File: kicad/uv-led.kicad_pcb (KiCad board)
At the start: 2 copper layers, 100 x 8 mm, 9 parts, among them J1 JST_PH_B2B-PH-K_1x02_P2.00mm_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

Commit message: added screw specs to silkscreen (#3)
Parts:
- H1, H2: footprint MountingHole:MountingHole_3.2mm_M3_DIN965_Pad_TopOnly -> MountingHole:MountingHole_3.2mm_M3_ISO14580_Pad_TopOnly
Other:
- board text added: "M3x10 ISO 14580 0.3 Nm"
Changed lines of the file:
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@@
 		(capping no)
 		(filling no)
-		(zone_defaults)
 		(pcbplotparams
 			(layerselection 0x00000000_00000000_55555555_5755f5ff)
@@
 		)
 	)
-	(footprint "MountingHole:MountingHole_3.2mm_M3_DIN965_Pad_TopOnly"
+	(footprint "MountingHole:MountingHole_3.2mm_M3_ISO14580_Pad_TopOnly"
 		(layer "F.Cu")
 		(at 190 100)
 		(descr "Mounting Hole 3.2mm, M3, generated by kicad-footprint-generator mountinghole.py")
-		(tags "mountinghole M3 DIN965")
+		(tags "mountinghole M3 ISO14580")
 		(property "Reference" "H2"
-			(at 5 0 0)
+			(at 0 -7 0)
 			(layer "F.SilkS")
 			(effects
@@
 		(property ki_fp_filters "MountingHole*Pad*")
 		(sheetname "/")
-		(sheetfile "uv-led-pcb.kicad_sch")
+		(sheetfile "uv-led.kicad_sch")
 		(units
 			(unit
@@
 		(fp_circle
 			(center 0 0)
-			(end 2.8 0)
+			(end 2.75 0)
 			(stroke
 				(width 0.15)
@@
 		(fp_circle
 			(center 0 0)
-			(end 3.05 0)
+			(end 3 0)
 			(stroke
 				(width 0.05)
@@
 		(pad "1" connect circle
 			(at 0 0)
-			(size 5.6 5.6)
+			(size 5.5 5.5)
 			(layers "F.Cu" "F.Mask")
 			(net "GND")
@@
 		(property ki_fp_filters "LED* LED_SMD:* LED_THT:*")
 		(sheetname "/")
-		(sheetfile "uv-led-pcb.kicad_sch")
+		(sheetfile "uv-led.kicad_sch")
 		(units
 			(unit
@@
 		(property ki_fp_filters "LED* LED_SMD:* LED_THT:*")
 		(sheetname "/")
-		(sheetfile "uv-led-pcb.kicad_sch")
+		(sheetfile "uv-led.kicad_sch")
 		(units
 			(unit
@@
 		(property ki_fp_filters "LED* LED_SMD:* LED_THT:*")
 		(sheetname "/")
-		(sheetfile "uv-led-pcb.kicad_sch")
+		(sheetfile "uv-led.kicad_sch")
 		(units
 			(unit
@@
 		(property ki_fp_filters "LED* LED_SMD:* LED_THT:*")
 		(sheetname "/")
-		(sheetfile "uv-led-pcb.kicad_sch")
+		(sheetfile "uv-led.kicad_sch")
 		(units
 			(unit
@@
 		(property ki_fp_filters "LED* LED_SMD:* LED_THT:*")
 		(sheetname "/")
-		(sheetfile "uv-led-pcb.kicad_sch")
+		(sheetfile "uv-led.kicad_sch")
 		(units
 			(unit
@@
 		)
 	)
-	(footprint "MountingHole:MountingHole_3.2mm_M3_DIN965_Pad_TopOnly"
+	(footprint "MountingHole:MountingHole_3.2mm_M3_ISO14580_Pad_TopOnly"
 		(layer "F.Cu")
 		(at 110 100)
 		(descr "Mounting Hole 3.2mm, M3, generated by kicad-footprint-generator mountinghole.py")
-		(tags "mountinghole M3 DIN965")
+		(tags "mountinghole M3 ISO14580")
 		(property "Reference" "H1"
-			(at -5 0 0)
+			(at 0 -5 0)
 			(layer "F.SilkS")
 			(effects
@@
 		(property ki_fp_filters "MountingHole*Pad*")
 		(sheetname "/")
-		(sheetfile "uv-led-pcb.kicad_sch")
+		(sheetfile "uv-led.kicad_sch")
 		(units
 			(unit
@@
 		(fp_circle
 			(center 0 0)
-			(end 2.8 0)
+			(end 2.75 0)
 			(stroke
 				(width 0.15)
@@
 		(fp_circle
 			(center 0 0)
-			(end 3.05 0)
+			(end 3 0)
 			(stroke
 				(width 0.05)
@@
 		(pad "1" connect circle
 			(at 0 0)
-			(size 5.6 5.6)
+			(size 5.5 5.5)
 			(layers "F.Cu" "F.Mask")
 			(net "GND")
@@
 		(property ki_fp_filters "R_*")
 		(sheetname "/")
-		(sheetfile "uv-led-pcb.kicad_sch")
+		(sheetfile "uv-led.kicad_sch")
 		(units
 			(unit
@@
 		(property ki_fp_filters "Connector*:*_1x??_*")
 		(sheetname "/")
-		(sheetfile "uv-led-pcb.kicad_sch")
+		(sheetfile "uv-led.kicad_sch")
 		(units
 			(unit
@@
 		(layer "Edge.Cuts")
 	)
+	(gr_text "M3x10\nISO 14580\n0.3 Nm"
+		(at 101.5 101.1 0)
+		(layer "F.SilkS")
+		(effects
+			(font
+				(size 0.5 0.5)
+				(thickness 0.1)
+			)
+			(justify left bottom)
+		)
+	)
+	(gr_text "M3x10\nISO 14580\n0.3 Nm"
+		(at 193.8 101.1 0)
+		(layer "F.SilkS")
+		(effects
+			(font
+				(size 0.5 0.5)
+				(thickness 0.1)
+			)
+			(justify left bottom)
+		)
+	)
 	(segment

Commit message: added recommended voltage / current and max current (#4)
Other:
- board text added: "20V / 0.5A max current: 1A"
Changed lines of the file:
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@@
+		)
+	)
+	(gr_text "20V / 0.5A\nmax current: 1A"
+		(at 117.4 101.2 0)
+		(layer "F.SilkS")
+		(effects
+			(font
+				(size 1 1)
+				(thickness 0.1)
+			)
+			(justify left bottom)
 		)
 	)

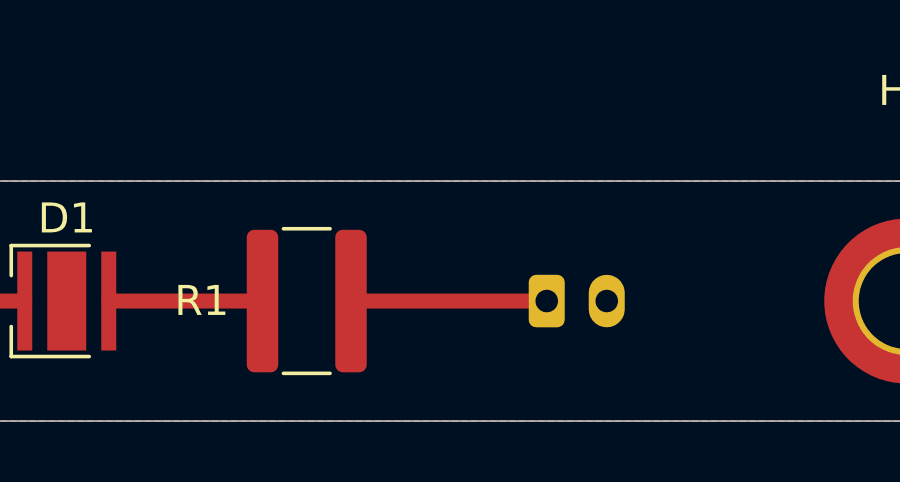
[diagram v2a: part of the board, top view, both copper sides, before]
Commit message: added polarity marker (+) on front and back silkscreen (#5)
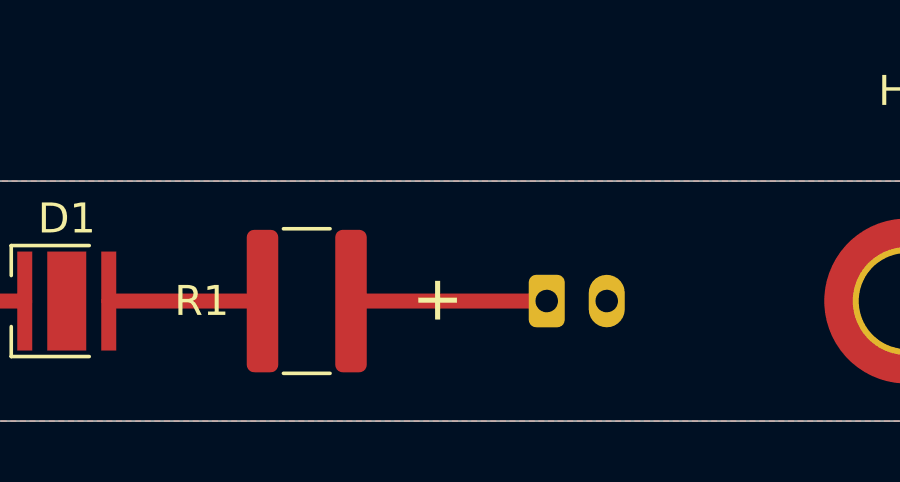
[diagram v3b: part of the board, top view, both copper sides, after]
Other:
- board text added: "+"
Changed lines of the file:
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@@
+		)
+	)
+	(gr_text "+"
+		(at 173.5 100.8 0)
+		(layer "F.SilkS")
+		(effects
+			(font
+				(size 1.5 1.5)
+				(thickness 0.1)
+			)
+			(justify left bottom)
+		)
+	)
+	(gr_text "+"
+		(at 175.5 100.8 0)
+		(layer "B.SilkS")
+		(effects
+			(font
+				(size 1.5 1.5)
+				(thickness 0.1)
+			)
+			(justify left bottom mirror)
 		)
 	)
